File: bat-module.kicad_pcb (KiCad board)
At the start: 2 copper layers, 86.3 x 91.9 mm, 5 parts

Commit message: preliminar model layout
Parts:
- added BT1: Battery, footprints:BATTERY_18650_STRIP_CONTACT, F.Cu at (53.0, 80.7)
- added BT2: Battery, footprints:BATTERY_18650_STRIP_CONTACT, F.Cu at (75.4, 80.7)
- added BT3: Battery, footprints:BATTERY_18650_STRIP_CONTACT, F.Cu at (97.8, 80.7)
- added BT4: Battery, footprints:BATTERY_18650_STRIP_CONTACT, F.Cu at (120.2, 80.7)
- added C1: 100nF, Capacitor_SMD:C_0603_1608Metric_Pad1.08x0.95mm_HandSolder, B.Cu at (127.5, 80.2)
- added C10: 100nF, Capacitor_SMD:C_0603_1608Metric_Pad1.08x0.95mm_HandSolder, B.Cu at (54.9, 67.8)
- added C11: 100nF, Capacitor_SMD:C_0603_1608Metric_Pad1.08x0.95mm_HandSolder, B.Cu at (55.4, 65.0)
- added C2: 3.3nF, Capacitor_SMD:C_0603_1608Metric_Pad1.08x0.95mm_HandSolder, B.Cu at (119.6, 67.2)
- added C27: 0.1uF/50V, Capacitor_SMD:C_0603_1608Metric_Pad1.08x0.95mm_HandSolder, B.Cu at (94.1, 110.2)
- added C28: 1000pF/50V, Capacitor_SMD:C_0603_1608Metric_Pad1.08x0.95mm_HandSolder, B.Cu at (75.4, 98.7)
- added C29: 1000pF/50V, Capacitor_SMD:C_0603_1608Metric_Pad1.08x0.95mm_HandSolder, B.Cu at (75.3, 102.8)
- added C3: 100pF, Capacitor_SMD:C_0603_1608Metric_Pad1.08x0.95mm_HandSolder, B.Cu at (119.6, 70.4)
- added C30: 0.47uF/50V, Capacitor_SMD:C_0603_1608Metric_Pad1.08x0.95mm_HandSolder, B.Cu at (76.0, 109.3)
- added C31: 0.1uF/50V, Capacitor_SMD:C_0603_1608Metric_Pad1.08x0.95mm_HandSolder, B.Cu at (91.6, 110.2)
- added C32: 100nF, Capacitor_SMD:C_0603_1608Metric_Pad1.08x0.95mm_HandSolder, B.Cu at (128.2, 102.1)
- added C33: 4.7uF, Capacitor_SMD:C_0603_1608Metric_Pad1.08x0.95mm_HandSolder, B.Cu at (120.1, 88.4)
- added C34: 47uF, Capacitor_SMD:C_0603_1608Metric_Pad1.08x0.95mm_HandSolder, B.Cu at (128.0, 90.5)
- added C35: 10uF, Capacitor_SMD:C_0603_1608Metric_Pad1.08x0.95mm_HandSolder, B.Cu at (127.5, 83.7)
- added C36: 10uF, Capacitor_SMD:C_0603_1608Metric_Pad1.08x0.95mm_HandSolder, B.Cu at (125.8, 83.7)
- added C37: 1uF, Capacitor_SMD:C_0603_1608Metric_Pad1.08x0.95mm_HandSolder, B.Cu at (124.2, 83.8)
- added C38: 22pF, Capacitor_SMD:C_0603_1608Metric_Pad1.08x0.95mm_HandSolder, B.Cu at (112.4, 56.9)
- added C39: 22uF, Capacitor_SMD:C_0603_1608Metric_Pad1.08x0.95mm_HandSolder, B.Cu at (121.3, 56.9)
- added C4: 1nF, Capacitor_SMD:C_0603_1608Metric_Pad1.08x0.95mm_HandSolder, B.Cu at (113.8, 71.6)
- added C40: 22uF, Capacitor_SMD:C_0603_1608Metric_Pad1.08x0.95mm_HandSolder, B.Cu at (123.0, 56.9)
- added C41: 22uF, Capacitor_SMD:C_0603_1608Metric_Pad1.08x0.95mm_HandSolder, B.Cu at (124.6, 56.9)
- added C5: 1nF, Capacitor_SMD:C_0603_1608Metric_Pad1.08x0.95mm_HandSolder, B.Cu at (112.2, 78.7)
- added C6: 100nF, Capacitor_SMD:C_0603_1608Metric_Pad1.08x0.95mm_HandSolder, B.Cu at (99.9, 66.6)
- added C7: 100nF, Capacitor_SMD:C_0603_1608Metric_Pad1.08x0.95mm_HandSolder, B.Cu at (99.3, 69.4)
- added C8: 100nF, Capacitor_SMD:C_0603_1608Metric_Pad1.08x0.95mm_HandSolder, B.Cu at (79.1, 71.9)
- added C9: 100nF, Capacitor_SMD:C_0603_1608Metric_Pad1.08x0.95mm_HandSolder, B.Cu at (78.1, 65.4)
- added D2: SS12FP, footprints:SS12FP, B.Cu at (120.2, 95.0)
- added D3: D_Schottky_Filled, footprints:NSVR0320MW2T1G, B.Cu at (81.4, 119.8)
- added Heater2: 20ppm/ ºC RS02B24R00FE12, footprints:RS02B24R00FE12, F.Cu at (109.0, 63.9)
- added Heater3: 20ppm/ ºC RS02B24R00FE12, footprints:RS02B24R00FE12, F.Cu at (86.6, 64.0)
- added Heater6: 20ppm/ ºC RS02B24R00FE12, footprints:RS02B24R00FE12, F.Cu at (64.2, 64.0)
- added IC3: DS2777G+, footprints:DS2777G+, B.Cu at (83.6, 110.5)
- added IC4: FDS6898AZ, footprints:FDS6898AZ, B.Cu at (83.6, 102.9)
- added J1: Conn_01x05_Socket, Connector_Molex:Molex_PicoBlade_53261-0571_1x05-1MP_P1.25mm_Horizontal, B.Cu at (112.9, 120.7)
- added J2: Conn_01x04_Socket, Connector_Molex:Molex_PicoBlade_53261-0471_1x04-1MP_P1.25mm_Horizontal, F.Cu at (103.8, 35.3)
- added J3: Conn_01x02_Socket, footprints:CON_2053380002, F.Cu at (87.9, 41.0)
- added J4: 61300311121, footprints:61300311121, B.Cu at (127.3, 56.2)
- added J7: Conn_01x04_Socket, Connector_Molex:Molex_PicoBlade_53261-0471_1x04-1MP_P1.25mm_Horizontal, F.Cu at (65.6, 35.3)
- added JP2: SolderJumper_2_Bridged, footprints:Jumper, B.Cu at (117.0, 74.9)
- added L2: 2.4uH, footprints:744325240, B.Cu at (120.7, 103.0)
- added Q4: SI2302DDS-T1-GE3, footprints:SI2302DDS-T1-GE3, B.Cu at (126.1, 67.4)
- added Q5: EPC2016C, footprints:EPC2016C, B.Cu at (126.4, 86.7)
- added Q6: EPC2016C, footprints:EPC2016C, B.Cu at (113.6, 86.7)
- added R10: 10R, Resistor_SMD:R_0603_1608Metric_Pad0.98x0.95mm_HandSolder, B.Cu at (113.1, 76.0)
- added R11: 8m, Resistor_SMD:R_2010_5025Metric_Pad1.40x2.65mm_HandSolder, B.Cu at (116.9, 56.8)
- added R12: 0.0R, Resistor_SMD:R_0603_1608Metric_Pad0.98x0.95mm_HandSolder, B.Cu at (127.5, 72.6)
- added R13: 90.9k, Resistor_SMD:R_0603_1608Metric_Pad0.98x0.95mm_HandSolder, B.Cu at (125.9, 72.6)
- added R14: 0.0R, Resistor_SMD:R_0603_1608Metric_Pad0.98x0.95mm_HandSolder, B.Cu at (113.7, 66.4)
- added R15: 20k, Resistor_SMD:R_0603_1608Metric_Pad0.98x0.95mm_HandSolder, B.Cu at (112.1, 66.4)
- added R17: 220k, Resistor_SMD:R_0603_1608Metric_Pad0.98x0.95mm_HandSolder, B.Cu at (96.3, 70.6)
- added R18: 10k, Resistor_SMD:R_0603_1608Metric_Pad0.98x0.95mm_HandSolder, B.Cu at (96.3, 68.2)
- added R19: 10k, Resistor_SMD:R_0603_1608Metric_Pad0.98x0.95mm_HandSolder, B.Cu at (96.3, 66.5)
- added R2: 100k, Resistor_SMD:R_0603_1608Metric_Pad0.98x0.95mm_HandSolder, B.Cu at (127.5, 62.1)
- added R20: 10k, Resistor_SMD:R_0603_1608Metric_Pad0.98x0.95mm_HandSolder, B.Cu at (100.8, 73.1)
- added R21: 10k, Resistor_SMD:R_0603_1608Metric_Pad0.98x0.95mm_HandSolder, B.Cu at (74.5, 65.4)
- added R22: 10k, Resistor_SMD:R_0603_1608Metric_Pad0.98x0.95mm_HandSolder, B.Cu at (74.5, 67.1)
- added R23: 10k, Resistor_SMD:R_0603_1608Metric_Pad0.98x0.95mm_HandSolder, B.Cu at (77.6, 68.1)
- added R24: 220k, Resistor_SMD:R_0603_1608Metric_Pad0.98x0.95mm_HandSolder, B.Cu at (74.5, 69.4)
- added R25: 10k, Resistor_SMD:R_0603_1608Metric_Pad0.98x0.95mm_HandSolder, B.Cu at (51.9, 65.0)
- added R26: 10k, Resistor_SMD:R_0603_1608Metric_Pad0.98x0.95mm_HandSolder, B.Cu at (51.9, 66.6)
- added R27: 10k, Resistor_SMD:R_0603_1608Metric_Pad0.98x0.95mm_HandSolder, B.Cu at (56.3, 71.6)
- added R28: 220k, Resistor_SMD:R_0603_1608Metric_Pad0.98x0.95mm_HandSolder, B.Cu at (51.9, 69.1)
- added R3: 2.2R, Resistor_SMD:R_0603_1608Metric_Pad0.98x0.95mm_HandSolder, B.Cu at (127.5, 76.1)
- added R4: 82k, Resistor_SMD:R_0603_1608Metric_Pad0.98x0.95mm_HandSolder, B.Cu at (112.1, 71.6)
- added R43: 150R, Resistor_SMD:R_0603_1608Metric_Pad0.98x0.95mm_HandSolder, B.Cu at (77.7, 109.2)
- added R44: 150R, Resistor_SMD:R_0603_1608Metric_Pad0.98x0.95mm_HandSolder, B.Cu at (72.4, 109.2)
- added R45: 1K, Resistor_SMD:R_0603_1608Metric_Pad0.98x0.95mm_HandSolder, B.Cu at (75.4, 104.5)
- added R46: 0R, Resistor_SMD:R_0603_1608Metric_Pad0.98x0.95mm_HandSolder, B.Cu at (74.2, 109.2)
- added R47: 1K, Resistor_SMD:R_0603_1608Metric_Pad0.98x0.95mm_HandSolder, B.Cu at (90.8, 105.4)
- added R48: 0R, Resistor_SMD:R_0603_1608Metric_Pad0.98x0.95mm_HandSolder, B.Cu at (78.8, 103.0)
- added R49: 470R, Resistor_SMD:R_0603_1608Metric_Pad0.98x0.95mm_HandSolder, B.Cu at (75.3, 101.0)
- added R5: 12k, Resistor_SMD:R_0603_1608Metric_Pad0.98x0.95mm_HandSolder, B.Cu at (119.6, 68.8)
- added R50: 1K, Resistor_SMD:R_0603_1608Metric_Pad0.98x0.95mm_HandSolder, B.Cu at (90.7, 103.6)
- added R51: 0R, Resistor_SMD:R_0603_1608Metric_Pad0.98x0.95mm_HandSolder, B.Cu at (90.7, 113.0)
- added R52: 150R, Resistor_SMD:R_0603_1608Metric_Pad0.98x0.95mm_HandSolder, B.Cu at (90.9, 107.2)
- added R53: 1K, Resistor_SMD:R_0603_1608Metric_Pad0.98x0.95mm_HandSolder, B.Cu at (83.4, 113.5)
- added R54: 150R, Resistor_SMD:R_0603_1608Metric_Pad0.98x0.95mm_HandSolder, B.Cu at (75.1, 112.4)
- added R55: 1K, Resistor_SMD:R_0603_1608Metric_Pad0.98x0.95mm_HandSolder, B.Cu at (89.9, 110.2)
- added R56: 10K, Resistor_SMD:R_0603_1608Metric_Pad0.98x0.95mm_HandSolder, B.Cu at (73.7, 118.7)
- added R57: 10K, Resistor_SMD:R_0603_1608Metric_Pad0.98x0.95mm_HandSolder, B.Cu at (76.3, 118.7)
- added R6: 100k, Resistor_SMD:R_0603_1608Metric_Pad0.98x0.95mm_HandSolder, B.Cu at (120.1, 86.7)
- added R7: 0.0R, Resistor_SMD:R_0603_1608Metric_Pad0.98x0.95mm_HandSolder, B.Cu at (125.9, 62.1)
- added R8: 10R, Resistor_SMD:R_0603_1608Metric_Pad0.98x0.95mm_HandSolder, B.Cu at (128.2, 97.6)
- added R9: 10R, Resistor_SMD:R_0603_1608Metric_Pad0.98x0.95mm_HandSolder, B.Cu at (112.5, 102.2)
- added RSense2: 0.01R/0.5W, Resistor_SMD:R_1206_3216Metric_Pad1.30x1.75mm_HandSolder, B.Cu at (83.4, 115.8)
- added RTD4: Thermistor, Resistor_SMD:R_1206_3216Metric_Pad1.30x1.75mm_HandSolder, F.Cu at (109.0, 80.5)
- added RTD5: Thermistor, Resistor_SMD:R_1206_3216Metric_Pad1.30x1.75mm_HandSolder, F.Cu at (86.6, 80.6)
- added RTD6: Thermistor, Resistor_SMD:R_1206_3216Metric_Pad1.30x1.75mm_HandSolder, F.Cu at (64.2, 80.6)
- added TP3: CC Test Point, TestPoint:TestPoint_Pad_D2.5mm, B.Cu at (98.0, 107.4)
- added TP4: DC Test Point, TestPoint:TestPoint_Pad_D2.5mm, B.Cu at (93.1, 100.4)
- added TP_COMMON1: TestPoint, TestPoint:TestPoint_Pad_D2.5mm, B.Cu at (91.5, 117.7)
- added TP_COMMON2: TestPoint, TestPoint:TestPoint_Pad_D2.5mm, B.Cu at (103.7, 118.1)
- added TP_COMMON3: TestPoint, TestPoint:TestPoint_Pad_D2.5mm, B.Cu at (65.1, 117.9)
- added U1: LM358, Package_SO:SOIC-8_3.9x4.9mm_P1.27mm, B.Cu at (97.2, 75.6)
- added U2: TPS22919QDCKRQ1, footprints:TPS22919QDCKRQ1, B.Cu at (97.2, 81.8)
- added U3: LM358, Package_SO:SOIC-8_3.9x4.9mm_P1.27mm, B.Cu at (75.4, 74.4)
- added U4: TPS22919QDCKRQ1, footprints:TPS22919QDCKRQ1, B.Cu at (75.4, 80.7)
- added U5: LM358, Package_SO:SOIC-8_3.9x4.9mm_P1.27mm, B.Cu at (52.8, 74.0)
- added U6: TPS22919QDCKRQ1, footprints:TPS22919QDCKRQ1, B.Cu at (52.7, 80.2)
- added U8: LTC3833EUDC-TRPBF, footprints:LTC3833EUDC#TRPBF, B.Cu at (119.9, 76.6)
- added Z2: 3SMAJ5919B-TP, footprints:3SMAJ5919B-TP, B.Cu at (71.0, 103.1)
- moved R1 4.31 mm to (120.2, 36.2), turned to -90 degrees
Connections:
- R1 pad 2: GND -> GNDREF
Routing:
- net /bat-monitoring/VBat_Common: track 0.00 -> 250.5 mm, vias 0 -> 2
- net /bat-monitoring/+VBat: track 0.00 -> 146.3 mm, vias 0 -> 4
- net /heater-circuit/RTD3: track 0.00 -> 134.1 mm, vias 0 -> 4
- net /batteries/+VBatB: track 0.00 -> 99.3 mm, vias 0 -> 3
- net /bat-monitoring/Veps+: track 0.00 -> 83.7 mm, vias 0 -> 4
- net /heater-circuit/RTD6: track 0.00 -> 75.4 mm, vias 0 -> 4
- net Heater_V3: track 0.00 -> 74.0 mm, vias 0 -> 1
- net Net-(Q5-Substrate): track 0.00 -> 73.9 mm, vias 0 -> 5
- net /batteries/3V3_A_~{EN}: track 0.00 -> 70.8 mm, vias 0 -> 3
- net /bat-monitoring/I2C0_SDA: track 0.00 -> 67.3 mm, vias 0 -> 3
- net /batteries/3V3_SENSE1+: track 0.00 -> 67.3 mm, vias 0 -> 2
- net /heater-circuit/RTD2: track 0.00 -> 62.2 mm, vias 0 -> 4
- net GNDREF: track 0.00 -> 61.9 mm, vias 0 -> 27
- net Heater_V6: track 0.00 -> 60.6 mm, vias 0 -> 1
- net /batteries/3V3: track 0.00 -> 58.0 mm, vias 0 -> 12
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- added copper zone on In1.Cu, net /batteries/3V3
- added copper zone on In2.Cu, net /batteries/3V3
- added copper zone on B.Cu, net GNDREF
- added copper zone on F.Cu, net GNDREF
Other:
- copper layers 2 -> 4

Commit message: fixing tracks and zones in DS2777G+
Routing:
- net Net-(IC3-VDD): track 16.0 -> 14.0 mm
- net Net-(IC3-DC): track 14.0 -> 12.2 mm
- net Net-(IC3-VB): track 31.8 -> 30.1 mm
- net /bat-monitoring/SRC: track 20.8 -> 19.4 mm
- net /bat-monitoring/V_sense0_P: track 11.3 -> 10.1 mm
- net /bat-monitoring/PIO: track 56.1 -> 57.3 mm
- net Net-(IC3-CC): track 10.4 -> 9.24 mm
- net Net-(IC3-SDA/DQ): track 12.6 -> 13.5 mm
- net Net-(IC3-CP): track 8.14 -> 7.26 mm
- net Net-(D3-K): track 51.7 -> 52.4 mm
- net /bat-monitoring/V_sense0_N: track 27.5 -> 28.1 mm
- added copper zone on B.Cu, net /bat-monitoring/SRC
- added copper zone on B.Cu, net /bat-monitoring/V_sense0_P
- added copper zone on B.Cu, net Net-(IC3-CC)
- added copper zone on B.Cu, net Net-(IC3-CP)
- added copper zone on B.Cu, net Net-(IC3-DC)
- added copper zone on B.Cu, net Net-(IC3-VB)
- added copper zone on B.Cu, net Net-(IC3-VDD)

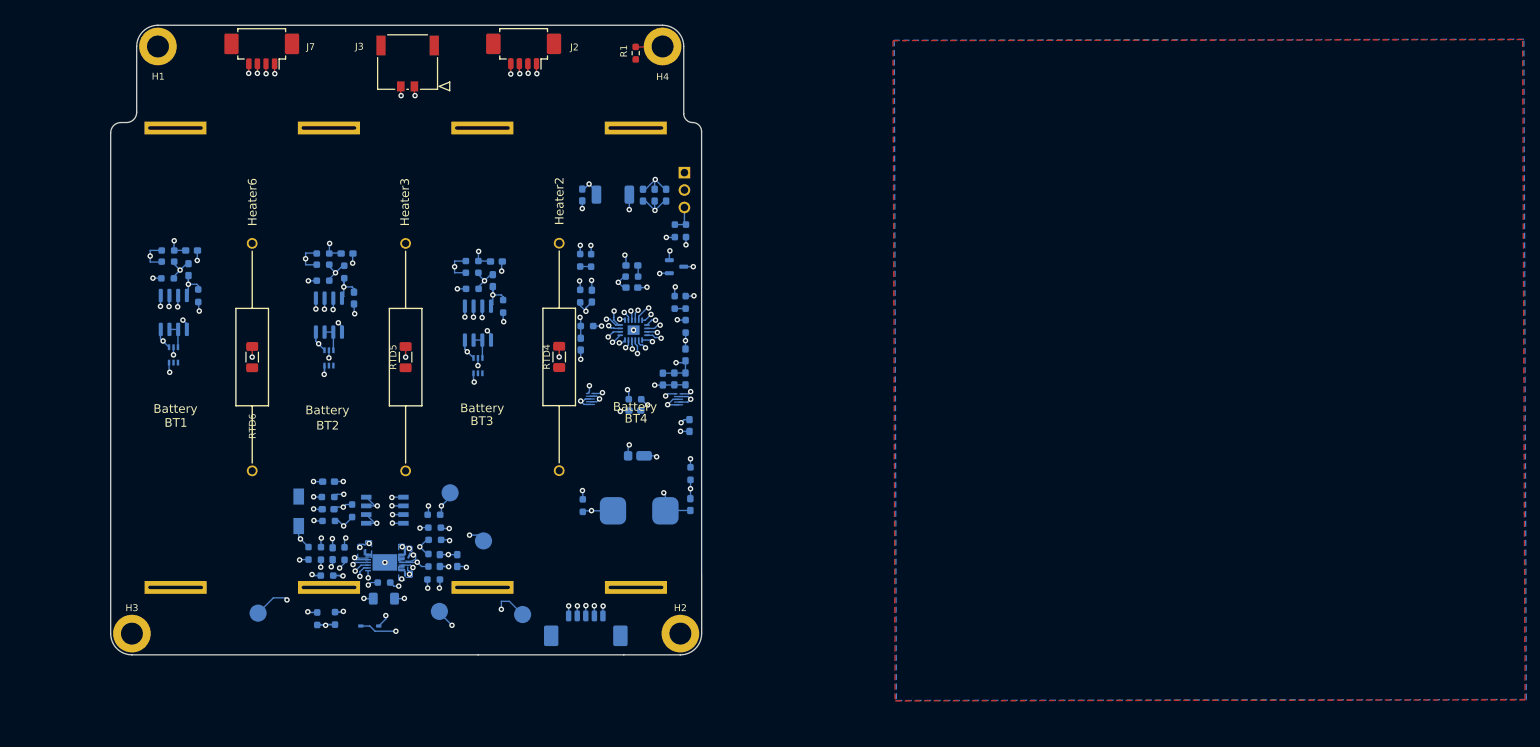
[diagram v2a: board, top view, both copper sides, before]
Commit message: retracing trails, changing footprints and improving circuit
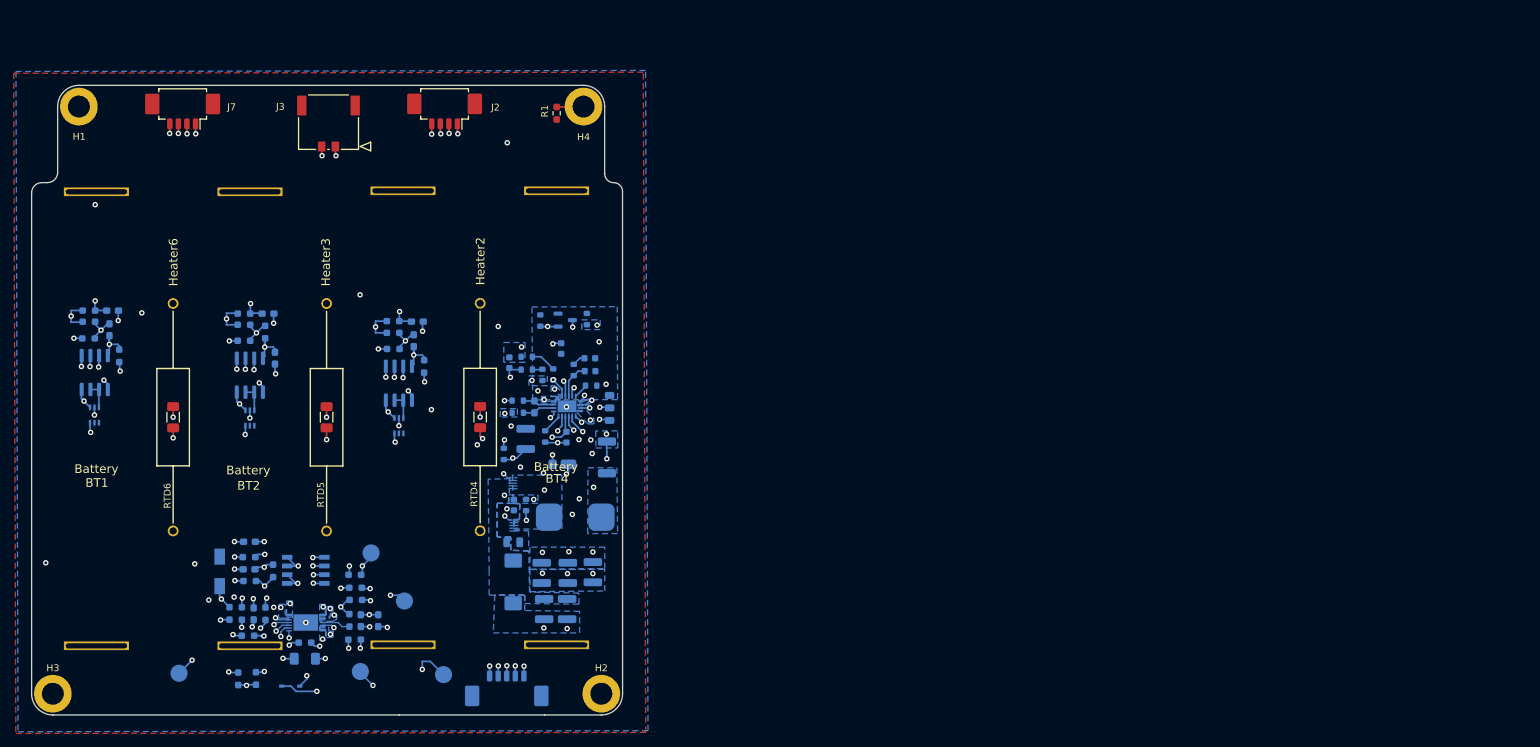
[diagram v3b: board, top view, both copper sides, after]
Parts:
- added ?: , footprints:2.5mm holes battery case mount, F.Cu at (168.6, 117.3)
- C1, C32: footprint Capacitor_SMD:C_0603_1608Metric_Pad1.08x0.95mm_HandSolder -> footprints:C0603C104K5RACTU
- C2: footprint Capacitor_SMD:C_0603_1608Metric_Pad1.08x0.95mm_HandSolder -> footprints:C0603C332J5GACAUTO
- C3: footprint Capacitor_SMD:C_0603_1608Metric_Pad1.08x0.95mm_HandSolder -> footprints:C0603C101J5GACAUTO
- C33: footprint Capacitor_SMD:C_0603_1608Metric_Pad1.08x0.95mm_HandSolder -> footprints:GCM32ER71H475KA55L
- C34: footprint Capacitor_SMD:C_0603_1608Metric_Pad1.08x0.95mm_HandSolder -> footprints:T495X476K035ATE300
- C35, C36: footprint Capacitor_SMD:C_0603_1608Metric_Pad1.08x0.95mm_HandSolder -> footprints:C1210C106K5RACTU
- C37: footprint Capacitor_SMD:C_0603_1608Metric_Pad1.08x0.95mm_HandSolder -> footprints:C0805C105K5RACTU
- C38: footprint Capacitor_SMD:C_0603_1608Metric_Pad1.08x0.95mm_HandSolder -> footprints:C0603C220K5RACAUTO
- C39, C40, C41: footprint Capacitor_SMD:C_0603_1608Metric_Pad1.08x0.95mm_HandSolder -> footprints:GCM32ER71C226KE19L
- C4: footprint Capacitor_SMD:C_0603_1608Metric_Pad1.08x0.95mm_HandSolder -> footprints:C0603C102F3GACTU
- J4: footprint footprints:61300311121 -> footprints:three_position_jumper
- R10, R8, R9: footprint Resistor_SMD:R_0603_1608Metric_Pad0.98x0.95mm_HandSolder -> footprints:CRCW060310R0FKEAHP
- R11: footprint Resistor_SMD:R_2010_5025Metric_Pad1.40x2.65mm_HandSolder -> footprints:WSL20108L000FEA18
- R12, R14, R7: footprint Resistor_SMD:R_0603_1608Metric_Pad0.98x0.95mm_HandSolder -> footprints:CRCW06030000Z0EAHP
- R13: footprint Resistor_SMD:R_0603_1608Metric_Pad0.98x0.95mm_HandSolder -> footprints:CRCW060390K9FKEAHP
- R15: footprint Resistor_SMD:R_0603_1608Metric_Pad0.98x0.95mm_HandSolder -> footprints:CRCW060320K0FKEAHP
- R2, R6: footprint Resistor_SMD:R_0603_1608Metric_Pad0.98x0.95mm_HandSolder -> footprints:CRCW0603100KFKEAHP
- R3: footprint Resistor_SMD:R_0603_1608Metric_Pad0.98x0.95mm_HandSolder -> footprints:CRCW06032R20FKEAHP
- R4: footprint Resistor_SMD:R_0603_1608Metric_Pad0.98x0.95mm_HandSolder -> footprints:CRCW060382K0FKEA
- R5: footprint Resistor_SMD:R_0603_1608Metric_Pad0.98x0.95mm_HandSolder -> footprints:CRCW060312K0FKEAHP
- moved C39 57.1 mm to (106.5, 112.0)
- moved C40 56.6 mm to (110.3, 112.0)
- moved C41 56.1 mm to (113.9, 111.9)
- moved C36 38.6 mm to (106.8, 117.3), turned to -90 degrees
- moved R11 38.4 mm to (116.0, 95.2), turned to -90 degrees
- moved C35 37.8 mm to (110.2, 117.3), turned to -90 degrees
- moved R3 35.0 mm to (104.2, 102.1), turned to -90 degrees
- moved C34 34.4 mm to (102.3, 113.4)
- moved J4 33.9 mm to (116.2, 88.3), turned to 90 degrees
- moved C1 33.3 mm to (102.4, 102.1)
- moved C37 32.3 mm to (102.3, 107.6), turned to 0 degrees
- moved Q5 27.1 mm to (102.3, 99.0)
- moved C38 26.7 mm to (101.7, 81.4)
- moved R2 25.0 mm to (106.3, 75.2)
- moved R12 24.5 mm to (104.3, 80.5), turned to 0 degrees
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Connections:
- BT1 pad 1: /batteries/+VBatB -> /bat-monitoring/VBat_Common
- BT2 pad 1: /bat-monitoring/VBat_Common -> /bat-monitoring/Bat2-
- BT3 pad 1: /bat-monitoring/VBat_Common -> /bat-monitoring/Bat2-
- BT4 pad 1: /bat-monitoring/+VBat -> /bat-monitoring/VBat_Common
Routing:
- net Net-(Q5-Substrate): track 73.9 -> 13.5 mm, vias 5 -> 2
- net /bat-monitoring/+VBat: track 146.3 -> 205.8 mm, vias 4 -> 6
- net GNDS: track 50.9 -> 0.00 mm, vias 5 -> 3
- net /batteries/3V3_SENSE1+: track 67.3 -> 26.3 mm, vias 2 -> 3
- net /batteries/3V3: track 58.0 -> 32.6 mm, vias 12 -> 14
- net Net-(U8-SENSE+): track 30.0 -> 4.71 mm, vias 3 -> 0
- net /heater-circuit/RTD3: track 134.1 -> 108.9 mm
- net /bat-monitoring/VBat_Common: track 250.5 -> 226.6 mm, vias 2 -> 3
- net Heater_V3: track 74.0 -> 50.1 mm, vias 1 -> 2
- net /batteries/3V3_VCC1: track 53.5 -> 32.3 mm, vias 4 -> 6
- net Net-(U8-BOOST): track 23.5 -> 2.93 mm, vias 2 -> 0
- net /batteries/VBUS_BK3V3: track 19.8 -> 0.00 mm, vias 3 -> 0
- net Net-(U8-RT): track 21.9 -> 2.16 mm, vias 2 -> 0
- net Net-(U8-VOSNS+): track 33.4 -> 13.7 mm, vias 4 -> 2
- net /batteries/3V3_SENSE1-: track 6.11 -> 25.4 mm, vias 2 -> 3
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- added copper zone on B.Cu, net /batteries/3V3
- added copper zone on B.Cu, net /batteries/3V3_SENSE1+
- added copper zone on B.Cu, net /batteries/VBUS_BK3V3
- added copper zone on B.Cu, net GNDS
- added copper zone on In1.Cu, net GNDS
- added copper zone on In2.Cu, net GNDS
- added copper zone on B.Cu, net Net-(Q5-Substrate)
- added copper zone on B.Cu, net Net-(U8-VIN)
- added copper zone on In1.Cu, net Net-(U8-VIN)
- added copper zone on In2.Cu, net Net-(U8-VIN)
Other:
- outline, holes or cut-outs redrawn
